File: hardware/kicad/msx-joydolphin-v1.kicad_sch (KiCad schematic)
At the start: 13 parts, among them J1 MSX Joystick, J2 GCN Joystick, J3 DEBUG, Q1 BSS138

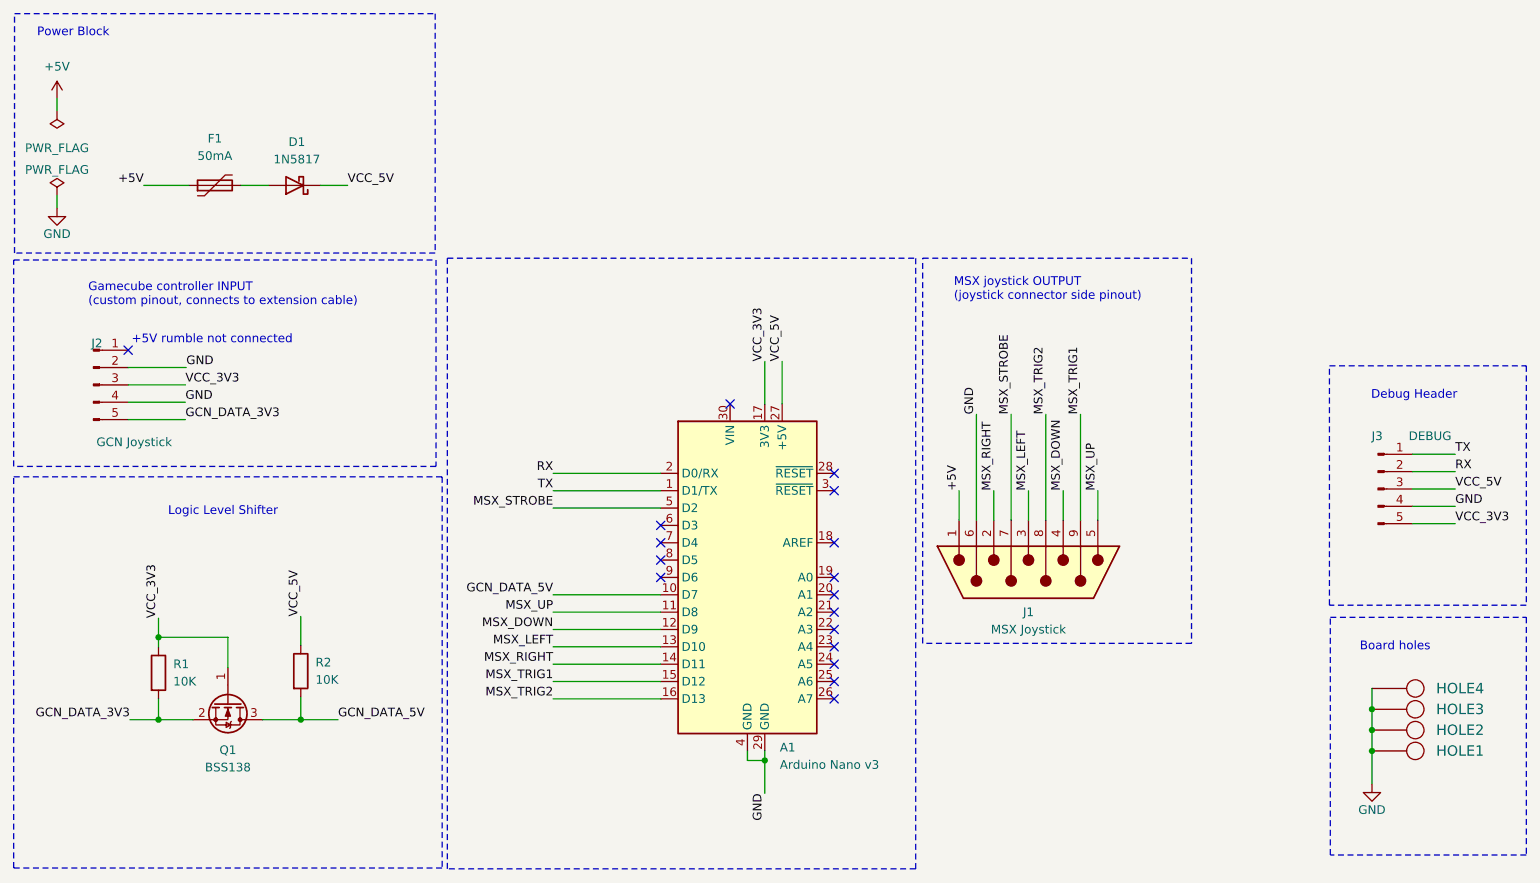
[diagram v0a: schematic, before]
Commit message: board: use OUT,TRGA,TRGB instead of STR,TRG1,TRG2
Signed-off-by: Albert Herranz <albert_herranz@yahoo.es>
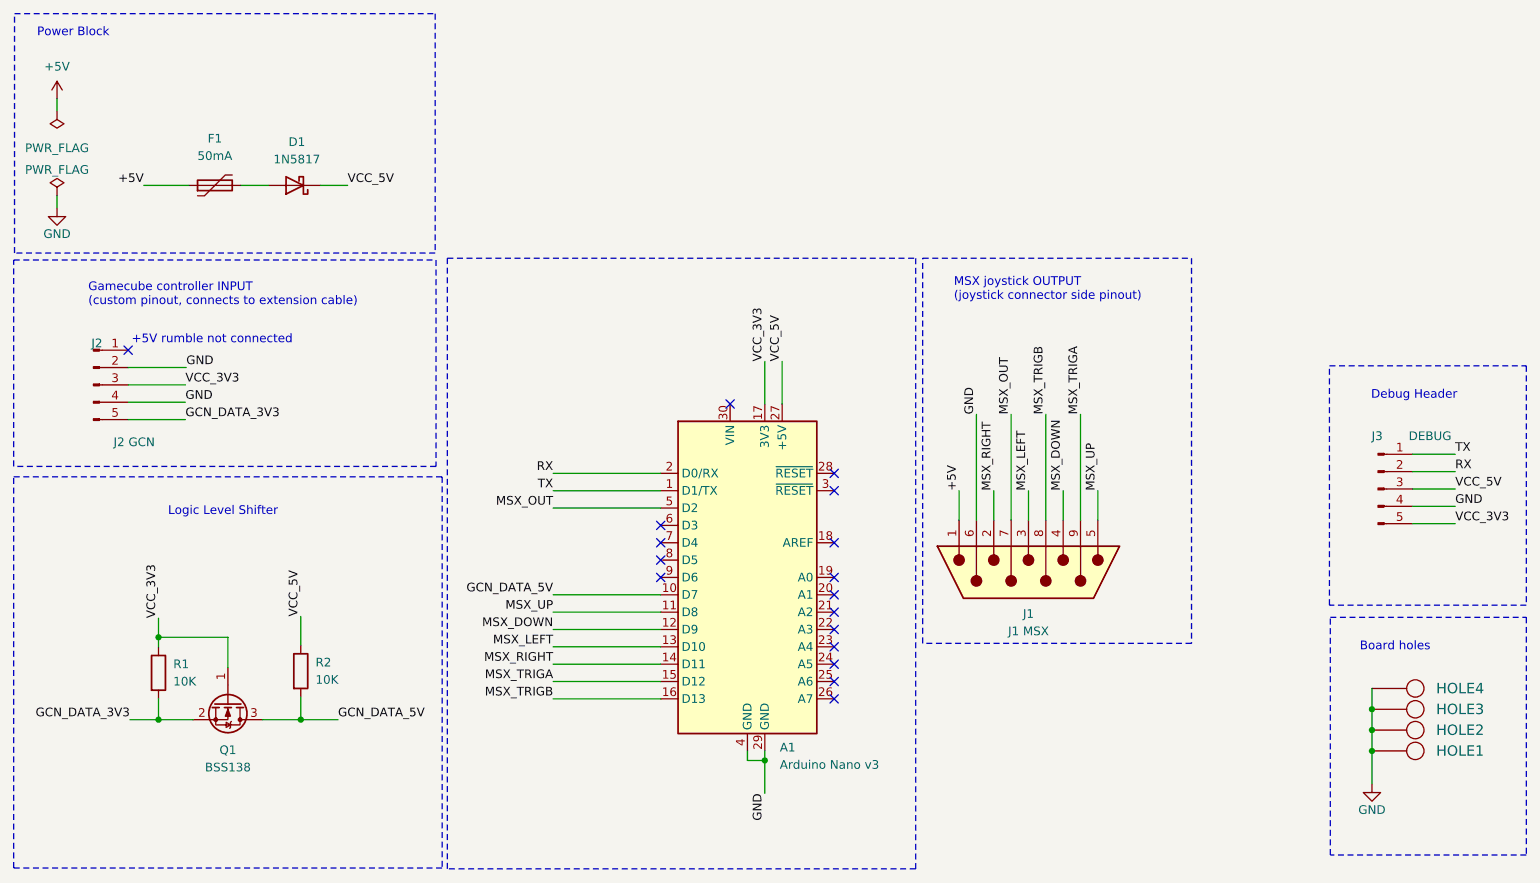
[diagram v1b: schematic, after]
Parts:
- J1: value MSX Joystick -> J1 MSX
- J2: value GCN Joystick -> J2 GCN
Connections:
- net MSX_STROBE renamed MSX_OUT
- net MSX_TRIG1 renamed MSX_TRIGA
- net MSX_TRIG2 renamed MSX_TRIGB
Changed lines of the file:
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@@
   (title_block
     (title "msx-joydolphin: A Gamecube controller adapter for MSX")
-    (date "2023-09-23")
-    (rev "v1")
+    (date "2024-02-21")
+    (rev "v1 Build1b")
     (company "Albert Herranz")
   )
@@
     (effects (font (size 1.27 1.27)) (justify left bottom))
   )
-  (label "MSX_TRIG2" (at 119.888 131.826 180) (fields_autoplaced)
+  (label "MSX_TRIGB" (at 119.888 131.826 180) (fields_autoplaced)
     (effects (font (size 1.27 1.27)) (justify right bottom))
   )
@@
     (effects (font (size 1.27 1.27)) (justify left bottom))
   )
-  (label "MSX_TRIG2" (at 192.024 90.17 90) (fields_autoplaced)
+  (label "MSX_TRIGB" (at 192.024 90.17 90) (fields_autoplaced)
     (effects (font (size 1.27 1.27)) (justify left bottom))
   )
@@
     (effects (font (size 1.27 1.27)) (justify left bottom))
   )
-  (label "MSX_STROBE" (at 119.888 103.886 180) (fields_autoplaced)
+  (label "MSX_OUT" (at 119.888 103.886 180) (fields_autoplaced)
     (effects (font (size 1.27 1.27)) (justify right bottom))
   )
@@
     (effects (font (size 1.27 1.27)) (justify left bottom))
   )
-  (label "MSX_TRIG1" (at 119.888 129.286 180) (fields_autoplaced)
+  (label "MSX_TRIGA" (at 119.888 129.286 180) (fields_autoplaced)
     (effects (font (size 1.27 1.27)) (justify right bottom))
   )
@@
     (effects (font (size 1.27 1.27)) (justify left bottom))
   )
-  (label "MSX_STROBE" (at 186.944 90.17 90) (fields_autoplaced)
+  (label "MSX_OUT" (at 186.944 90.17 90) (fields_autoplaced)
     (effects (font (size 1.27 1.27)) (justify left bottom))
   )
@@
     (effects (font (size 1.27 1.27)) (justify left bottom))
   )
-  (label "MSX_TRIG1" (at 197.104 90.17 90) (fields_autoplaced)
+  (label "MSX_TRIGA" (at 197.104 90.17 90) (fields_autoplaced)
     (effects (font (size 1.27 1.27)) (justify left bottom))
   )
@@
   (symbol (lib_id "Connector:DE9_Plug") (at 189.484 113.284 270) (unit 1)
     (in_bom yes) (on_board yes) (dnp no) (fields_autoplaced)
-    (property "Reference" "J1" (at 189.484 119.126 90)
-      (effects (font (size 1.27 1.27)))
-    )
-    (property "Value" "MSX Joystick" (at 189.484 121.666 90)
+    (property "Reference" "J1" (at 189.484 119.38 90)
+      (effects (font (size 1.27 1.27)))
+    )
+    (property "Value" "J1 MSX" (at 189.484 121.92 90)
       (effects (font (size 1.27 1.27)))
     )
@@
       (effects (font (size 1.27 1.27)))
     )
-    (property "Value" "GCN Joystick" (at 58.547 94.234 0)
-      (effects (font (size 1.27 1.27)))
-    )
+    (property "Value" "J2 GCN" (at 58.547 94.234 0)
+      (effects (font (size 1.27 1.27)))
+    )
